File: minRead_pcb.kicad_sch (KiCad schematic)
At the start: 117 parts, among them J1 USB_C_Receptacle, J2 FH34SRJ-24S-0.5SH_50_, J3 FH34SRJ-6S-0.5SH_50_, J5 Conn_01x02, J7 Micro_SD_Card, Q10 BSS138, Q11 BSS138, Q16 MMBT3906, Q17 MMBT3904, Q18 AO3419, Q4 [BSS138] AO3400A, Q5 AO3419, Q6 AO3419, SW1 SW_Push, SW10 SW_Push, SW11 SW_Push, SW2 SW_Push, SW3 SW_Push, SW4 SW_Push, SW6 SW_Push, SW8 SW_Push, SW9 SW_Push, U1 TPD4E1U06DBVR, U11 AP3031KTR, U3 AP2112K-3.3, U4 ESP32-S3-WROOM-1, U6 TPD4E1U06DBVR, U7 MCP73832-2-OT

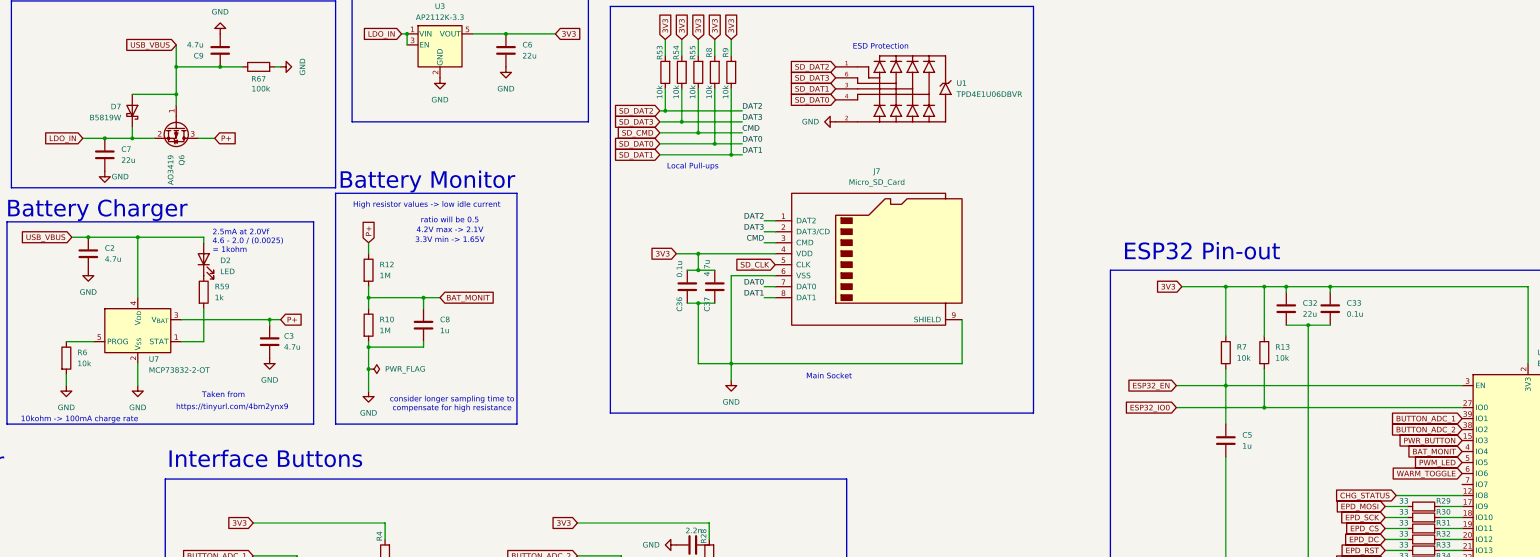
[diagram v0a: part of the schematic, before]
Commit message: implement charge pump
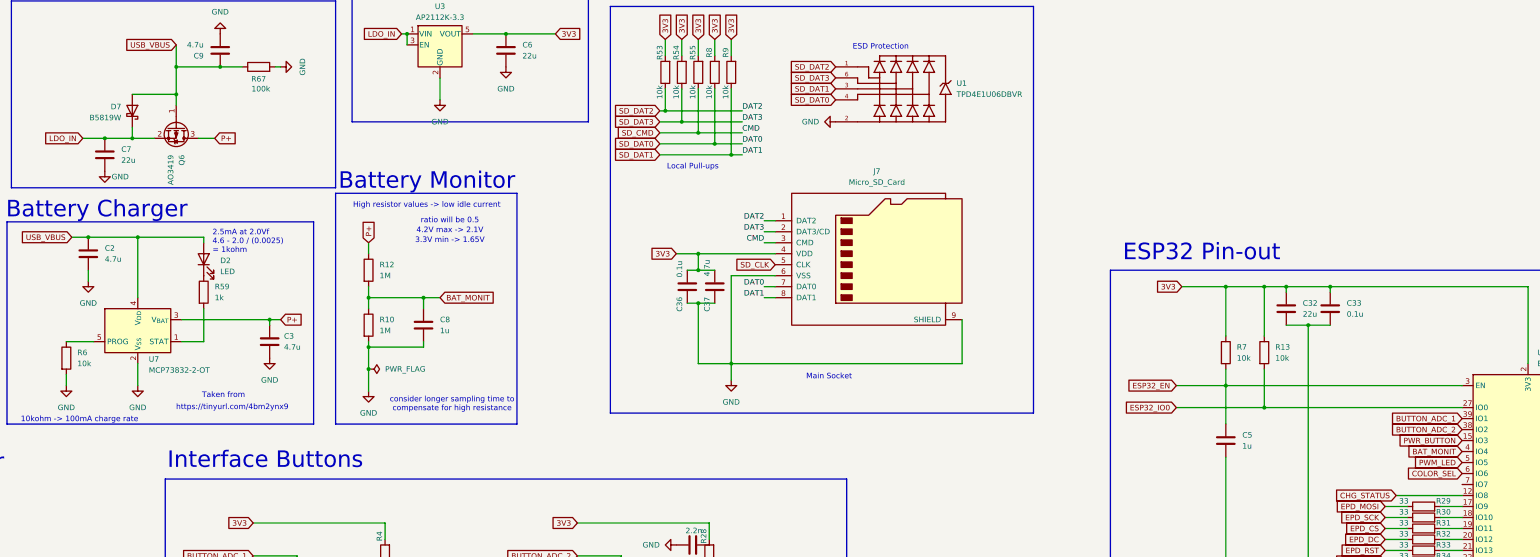
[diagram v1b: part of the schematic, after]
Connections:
- net WARM_TOGGLE is gone; now on net COLOR_SEL: U4.6 (IO6)
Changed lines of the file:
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@@
 	(wire
 		(pts
+			(xy 196.85 52.07) (xy 196.85 46.99)
+		)
+		(stroke
+			(width 0)
+			(type default)
+		)
+	)
+	(wire
+		(pts
 			(xy 261.62 266.7) (xy 264.16 266.7)
 		)
@@
 	(wire
 		(pts
+			(xy 115.57 93.98) (xy 115.57 91.44)
+		)
+		(stroke
+			(width 0)
+			(type default)
+		)
+	)
+	(wire
+		(pts
 			(xy 96.52 288.29) (xy 86.36 288.29)
 		)
@@
 		)
 	)
-	(global_label "PWR_BUTTON"
+	(global_label "COLOR_SEL"
 		(shape input)
-		(at 49.53 353.06 0)
+		(at 433.07 138.43 180)
 		(fields_autoplaced yes)
 		(effects
@@
 				(size 1.27 1.27)
 			)
-			(justify left)
+			(justify right)
 		)
 		(property "Intersheetrefs" "${INTERSHEET_REFS}"
-			(at 64.6709 353.06 0)
+			(at 419.5015 138.43 0)
 			(hide yes)
 			(show_name no)
@@
 					(size 1.27 1.27)
 				)
-				(justify left)
+				(justify right)
 			)
 		)
 	)
-	(global_label "ESP32_EN"
+	(global_label "PWR_BUTTON"
 		(shape input)
-		(at 367.03 118.11 180)
+		(at 49.53 353.06 0)
 		(fields_autoplaced yes)
 		(effects
@@
 				(size 1.27 1.27)
 			)
-			(justify right)
+			(justify left)
 		)
 		(property "Intersheetrefs" "${INTERSHEET_REFS}"
-			(at 359.5418 118.11 0)
+			(at 64.6709 353.06 0)
 			(hide yes)
 			(show_name no)
@@
 					(size 1.27 1.27)
 				)
-				(justify right)
+				(justify left)
 			)
 		)
 	)
-	(global_label "ESP32_IO0"
+	(global_label "ESP32_EN"
 		(shape input)
-		(at 367.03 123.19 180)
+		(at 367.03 118.11 180)
 		(fields_autoplaced yes)
 		(effects
@@
 		)
 		(property "Intersheetrefs" "${INTERSHEET_REFS}"
-			(at 353.8849 123.19 0)
+			(at 359.5418 118.11 0)
 			(hide yes)
 			(show_name no)
@@
 		)
 	)
-	(global_label "BUTTON_ADC_1"
+	(global_label "ESP32_IO0"
 		(shape input)
-		(at 433.07 125.73 180)
+		(at 367.03 123.19 180)
 		(fields_autoplaced yes)
 		(effects
@@
 		)
 		(property "Intersheetrefs" "${INTERSHEET_REFS}"
-			(at 416.1148 125.73 0)
+			(at 353.8849 123.19 0)
 			(hide yes)
 			(show_name no)
@@
 		)
 	)
-	(global_label "LED_SW"
+	(global_label "BUTTON_ADC_1"
 		(shape input)
-		(at 217.17 280.67 180)
+		(at 433.07 125.73 180)
 		(fields_autoplaced yes)
 		(effects
@@
 		)
 		(property "Intersheetrefs" "${INTERSHEET_REFS}"
-			(at 207.1092 280.67 0)
+			(at 416.1148 125.73 0)
 			(hide yes)
 			(show_name no)
@@
 		)
 	)
-	(global_label "WARM_TOGGLE"
+	(global_label "LED_SW"
 		(shape input)
-		(at 433.07 138.43 180)
+		(at 217.17 280.67 180)
 		(fields_autoplaced yes)
 		(effects
@@
 		)
 		(property "Intersheetrefs" "${INTERSHEET_REFS}"
-			(at 416.8406 138.43 0)
+			(at 207.1092 280.67 0)
 			(hide yes)
 			(show_name no)
@@
 		(length 2.54)
 		(shape round)
+		(at 196.85 50.8 270)
+		(fields_autoplaced yes)
+		(effects
+			(font
+				(size 1.27 1.27)
+			)
+			(justify right bottom)
+		)
+		(property "Netclass" "3V3"
+			(at 199.39 50.1015 90)
+			(show_name no)
+			(do_not_autoplace no)
+			(effects
+				(font
+					(size 1.27 1.27)
+				)
+				(justify left)
+			)
+		)
+		(property "Component Class" ""
+			(at -22.86 -199.39 0)
+			(show_name no)
+			(do_not_autoplace no)
+			(effects
+				(font
+					(size 1.27 1.27)
+					(italic yes)
+				)
+			)
+		)
+	)
+	(netclass_flag ""
+		(length 2.54)
+		(shape round)
 		(at 48.26 30.48 180)
 		(fields_autoplaced yes)
@@
 		(in_pos_files yes)
 		(dnp no)
-		(fields_autoplaced yes)
 		(property "Reference" "#PWR049"
 			(at 166.37 44.45 0)
@@
 	(symbol
 		(lib_id "power:GND")
-		(at 115.57 91.44 0)
+		(at 115.57 93.98 0)
 		(unit 1)
 		(body_style 1)
@@
 		(fields_autoplaced yes)
 		(property "Reference" "#PWR021"
-			(at 115.57 97.79 0)
+			(at 115.57 100.33 0)
 			(hide yes)
 			(show_name no)
@@
 		)
 		(property "Value" "GND"
-			(at 115.57 96.52 0)
+			(at 115.57 99.06 0)
 			(show_name no)
 			(do_not_autoplace no)
@@
 		)
 		(property "Footprint" ""
-			(at 115.57 91.44 0)
+			(at 115.57 93.98 0)
 			(hide yes)
 			(show_name no)
@@
 		)
 		(property "Datasheet" ""
-			(at 115.57 91.44 0)
+			(at 115.57 93.98 0)
 			(hide yes)
 			(show_name no)
@@
 		)
 		(property "Description" "Power symbol creates a global label with name \"GND\" , ground"
-			(at 115.57 91.44 0)
+			(at 115.57 93.98 0)
 			(hide yes)
 			(show_name no)
@@
 	(symbol
 		(lib_id "power:GND")
-		(at 196.85 46.99 0)
+		(at 196.85 52.07 0)
 		(unit 1)
 		(body_style 1)
@@
 		(fields_autoplaced yes)
 		(property "Reference" "#PWR027"
-			(at 196.85 53.34 0)
+			(at 196.85 58.42 0)
 			(hide yes)
 			(show_name no)
@@
 		)
 		(property "Value" "GND"
-			(at 196.85 52.07 0)
+			(at 196.85 57.15 0)
 			(show_name no)
 			(do_not_autoplace no)
@@
 		)
 		(property "Footprint" ""
-			(at 196.85 46.99 0)
+			(at 196.85 52.07 0)
 			(hide yes)
 			(show_name no)
@@
 		)
 		(property "Datasheet" ""
-			(at 196.85 46.99 0)
+			(at 196.85 52.07 0)
 			(hide yes)
 			(show_name no)
@@
 		)
 		(property "Description" "Power symbol creates a global label with name \"GND\" , ground"
-			(at 196.85 46.99 0)
+			(at 196.85 52.07 0)
 			(hide yes)
 			(show_name no)

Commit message: light bar circuit mostly routed
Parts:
- SW6: now fitted
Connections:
- net LED_PWR is gone; now on net LED_ACTIVATE: U4.10 (IO17)
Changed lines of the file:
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@@
 		)
 	)
-	(global_label "LED_PWR"
+	(global_label "LED_ACTIVATE"
 		(shape input)
 		(at 463.55 123.19 0)
@@
 		)
 		(property "Intersheetrefs" "${INTERSHEET_REFS}"
-			(at 474.9413 123.19 0)
+			(at 479.1747 123.19 0)
 			(hide yes)
 			(show_name no)
@@
 		(length 2.54)
 		(shape round)
-		(at 196.85 50.8 270)
-		(fields_autoplaced yes)
-		(effects
-			(font
-				(size 1.27 1.27)
-			)
-			(justify right bottom)
-		)
-		(property "Netclass" "3V3"
-			(at 199.39 50.1015 90)
-			(show_name no)
-			(do_not_autoplace no)
-			(effects
-				(font
-					(size 1.27 1.27)
-				)
-				(justify left)
-			)
-		)
-		(property "Component Class" ""
-			(at -22.86 -199.39 0)
-			(show_name no)
-			(do_not_autoplace no)
-			(effects
-				(font
-					(size 1.27 1.27)
-					(italic yes)
-				)
-			)
-		)
-	)
-	(netclass_flag ""
-		(length 2.54)
-		(shape round)
 		(at 48.26 30.48 180)
 		(fields_autoplaced yes)
@@
 		(length 2.54)
 		(shape round)
-		(at 293.37 299.72 180)
-		(fields_autoplaced yes)
-		(effects
-			(font
-				(size 1.27 1.27)
-			)
-			(justify right bottom)
-		)
-		(property "Netclass" "3V3"
-			(at 294.0685 302.26 0)
-			(show_name no)
-			(do_not_autoplace no)
-			(effects
-				(font
-					(size 1.27 1.27)
-				)
-				(justify left)
-			)
-		)
-		(property "Component Class" ""
-			(at 33.02 29.21 0)
-			(show_name no)
-			(do_not_autoplace no)
-			(effects
-				(font
-					(size 1.27 1.27)
-					(italic yes)
-				)
-			)
-		)
-	)
-	(netclass_flag ""
-		(length 2.54)
-		(shape round)
 		(at 66.04 288.29 90)
 		(fields_autoplaced yes)
@@
 		(length 2.54)
 		(shape round)
-		(at 66.04 270.51 90)
-		(fields_autoplaced yes)
-		(effects
-			(font
-				(size 1.27 1.27)
-			)
-			(justify left bottom)
-		)
-		(property "Netclass" "3V3"
-			(at 63.5 269.8115 90)
-			(show_name no)
-			(do_not_autoplace no)
-			(effects
-				(font
-					(size 1.27 1.27)
-				)
-				(justify left)
-			)
-		)
-		(property "Component Class" ""
-			(at -153.67 20.32 0)
-			(show_name no)
-			(do_not_autoplace no)
-			(effects
-				(font
-					(size 1.27 1.27)
-					(italic yes)
-				)
-			)
-		)
-	)
-	(netclass_flag ""
-		(length 2.54)
-		(shape round)
 		(at 58.42 30.48 180)
 		(fields_autoplaced yes)
@@
 		)
 	)
-	(netclass_flag ""
-		(length 2.54)
-		(shape round)
-		(at 346.71 299.72 0)
-		(fields_autoplaced yes)
-		(effects
-			(font
-				(size 1.27 1.27)
-			)
-			(justify left bottom)
-		)
-		(property "Netclass" "3V3"
-			(at 347.4085 297.18 0)
-			(show_name no)
-			(do_not_autoplace no)
-			(effects
-				(font
-					(size 1.27 1.27)
-				)
-				(justify left)
-			)
-		)
-		(property "Component Class" ""
-			(at 86.36 29.21 0)
-			(show_name no)
-			(do_not_autoplace no)
-			(effects
-				(font
-					(size 1.27 1.27)
-					(italic yes)
-				)
-			)
-		)
-	)
 	(symbol
 		(lib_id "Device:C")
@@
 		(on_board yes)
 		(in_pos_files yes)
-		(dnp yes)
+		(dnp no)
 		(fields_autoplaced yes)
 		(property "Reference" "SW6"

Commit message: reverse mount buttons
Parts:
- SW2, SW3, SW8, SW9: footprint mjtp1117:MJTP1117 -> DEAN:SKQGABE010_ALPS_Reverse
- SW6: footprint Button_Switch_THT:SW_PUSH_6mm -> Button_Switch_THT:SW_PUSH_1P1T_6x3.5mm_H4.3_APEM_MJTP1243; now not fitted
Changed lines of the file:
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@@
 	)
 	(symbol
+		(lib_name "SW_Push_1")
 		(lib_id "Switch:SW_Push")
 		(at 163.83 189.23 90)
@@
 			)
 		)
-		(property "Footprint" "mjtp1117:MJTP1117"
+		(property "Footprint" "DEAN:SKQGABE010_ALPS_Reverse"
 			(at 158.75 189.23 0)
 			(hide yes)
@@
 			)
 		)
-		(property "Footprint" "mjtp1117:MJTP1117"
+		(property "Footprint" "DEAN:SKQGABE010_ALPS_Reverse"
 			(at 172.72 189.23 0)
 			(hide yes)
@@
 			)
 		)
-		(property "Footprint" "mjtp1117:MJTP1117"
+		(property "Footprint" "DEAN:SKQGABE010_ALPS_Reverse"
 			(at 185.42 189.23 0)
 			(hide yes)
@@
 			)
 		)
-		(property "Footprint" "mjtp1117:MJTP1117"
+		(property "Footprint" "DEAN:SKQGABE010_ALPS_Reverse"
 			(at 196.85 189.23 0)
 			(hide yes)
@@
 		(on_board yes)
 		(in_pos_files yes)
-		(dnp no)
+		(dnp yes)
 		(fields_autoplaced yes)
 		(property "Reference" "SW6"
@@
 			)
 		)
-		(property "Footprint" "Button_Switch_THT:SW_PUSH_6mm"
+		(property "Footprint" "Button_Switch_THT:SW_PUSH_1P1T_6x3.5mm_H4.3_APEM_MJTP1243"
 			(at 107.95 347.98 0)
 			(hide yes)

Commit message: switch buttons to mid mount
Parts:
- added C12: 1u, Capacitor_SMD:C_0805_2012Metric_Pad1.18x1.45mm_HandSolder, symbol Device:C
- C6: value 22u -> 1u
- D2: footprint LED_THT:LED_D3.0mm -> LED_SMD:LED_0805_2012Metric_Pad1.15x1.40mm_HandSolder
- SW1, SW10, SW4: footprint mjtp1117:MJTP1117 -> DEAN:SKSNLAE010
- SW11: footprint mjtp1117:MJTP1117 -> TestPoint:TestPoint_Bridge_Pitch2.54mm_Drill1.0mm
- SW6: footprint Button_Switch_THT:SW_PUSH_1P1T_6x3.5mm_H4.3_APEM_MJTP1243 -> TestPoint:TestPoint_Bridge_Pitch2.54mm_Drill1.0mm
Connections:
- net GND: now also C12.2
- net LDO_IN: now also C12.1
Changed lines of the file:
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@@
 	)
 	(rectangle
-		(start 176.53 27.94)
+		(start 176.53 21.59)
 		(end 231.14 57.15)
 		(stroke
@@
 	(text "LDO 3.3V"
 		(exclude_from_sim no)
-		(at 177.292 25.654 0)
+		(at 177.038 16.002 0)
 		(effects
 			(font
@@
 	(wire
 		(pts
+			(xy 215.9 273.05) (xy 218.44 273.05)
+		)
+		(stroke
+			(width 0)
+			(type default)
+		)
+	)
+	(wire
+		(pts
 			(xy 142.24 100.33) (xy 142.24 107.95)
 		)
@@
 	(wire
 		(pts
-			(xy 217.17 283.21) (xy 218.44 283.21)
+			(xy 214.63 283.21) (xy 218.44 283.21)
 		)
 		(stroke
@@
 	(global_label "C-"
 		(shape input)
-		(at 218.44 273.05 180)
+		(at 215.9 273.05 180)
 		(fields_autoplaced yes)
 		(effects
@@
 		)
 		(property "Intersheetrefs" "${INTERSHEET_REFS}"
-			(at 212.6124 273.05 0)
+			(at 210.0724 273.05 0)
 			(hide yes)
 			(show_name no)
@@
 	(global_label "W-"
 		(shape input)
-		(at 217.17 283.21 180)
+		(at 214.63 283.21 180)
 		(fields_autoplaced yes)
 		(effects
@@
 		)
 		(property "Intersheetrefs" "${INTERSHEET_REFS}"
-			(at 211.161 283.21 0)
+			(at 208.621 283.21 0)
 			(hide yes)
 			(show_name no)
@@
 		(length 2.54)
 		(shape round)
-		(at 48.26 30.48 180)
-		(fields_autoplaced yes)
-		(effects
-			(font
-				(size 1.27 1.27)
-			)
-			(justify right bottom)
-		)
-		(property "Netclass" "3V3"
-			(at 48.9585 33.02 0)
-			(show_name no)
-			(do_not_autoplace no)
-			(effects
-				(font
-					(size 1.27 1.27)
-				)
-				(justify left)
-			)
-		)
-		(property "Component Class" ""
-			(at -171.45 -219.71 0)
-			(show_name no)
-			(do_not_autoplace no)
-			(effects
-				(font
-					(size 1.27 1.27)
-					(italic yes)
-				)
-			)
-		)
-	)
-	(netclass_flag ""
-		(length 2.54)
-		(shape round)
 		(at 284.48 266.7 180)
 		(fields_autoplaced yes)
@@
 		(length 2.54)
 		(shape round)
-		(at 304.8 289.56 0)
-		(fields_autoplaced yes)
-		(effects
-			(font
-				(size 1.27 1.27)
-			)
-			(justify left bottom)
-		)
-		(property "Netclass" "3V3"
-			(at 305.4985 287.02 0)
-			(show_name no)
-			(do_not_autoplace no)
-			(effects
-				(font
-					(size 1.27 1.27)
-				)
-				(justify left)
-			)
-		)
-		(property "Component Class" ""
-			(at 44.45 19.05 0)
-			(show_name no)
-			(do_not_autoplace no)
-			(effects
-				(font
-					(size 1.27 1.27)
-					(italic yes)
-				)
-			)
-		)
-	)
-	(netclass_flag ""
-		(length 2.54)
-		(shape round)
 		(at 49.53 297.18 0)
 		(fields_autoplaced yes)
@@
 			)
 		)
-		(property "Footprint" "mjtp1117:MJTP1117"
+		(property "Footprint" "TestPoint:TestPoint_Bridge_Pitch2.54mm_Drill1.0mm"
 			(at 109.22 372.11 0)
 			(hide yes)
@@
 			)
 		)
-		(property "Footprint" "mjtp1117:MJTP1117"
+		(property "Footprint" "DEAN:SKSNLAE010"
 			(at 233.68 189.23 0)
 			(hide yes)
@@
 	(symbol
 		(lib_id "power:GND")
+		(at 189.23 29.21 180)
+		(unit 1)
+		(body_style 1)
+		(exclude_from_sim no)
+		(in_bom yes)
+		(on_board yes)
+		(in_pos_files yes)
+		(dnp no)
+		(fields_autoplaced yes)
+		(property "Reference" "#PWR028"
+			(at 189.23 22.86 0)
+			(hide yes)
+			(show_name no)
+			(do_not_autoplace no)
+			(effects
+				(font
+					(size 1.27 1.27)
+				)
+			)
+		)
+		(property "Value" "GND"
+			(at 189.23 24.13 0)
+			(show_name no)
+			(do_not_autoplace no)
+			(effects
+				(font
+					(size 1.27 1.27)
+				)
+			)
+		)
+		(property "Footprint" ""
+			(at 189.23 29.21 0)
+			(hide yes)
+			(show_name no)
+			(do_not_autoplace no)
+			(effects
+				(font
+					(size 1.27 1.27)
+				)
+			)
+		)
+		(property "Datasheet" ""
+			(at 189.23 29.21 0)
+			(hide yes)
+			(show_name no)
+			(do_not_autoplace no)
+			(effects
+				(font
+					(size 1.27 1.27)
+				)
+			)
+		)
+		(property "Description" "Power symbol creates a global label with name \"GND\" , ground"
+			(at 189.23 29.21 0)
+			(hide yes)
+			(show_name no)
+			(do_not_autoplace no)
+			(effects
+				(font
+					(size 1.27 1.27)
+				)
+			)
+		)
+		(pin "1"
+		)
+		(instances
+			(project "minRead_pcb"
+				(path "/2fbd4c8f-b784-4d80-b374-4947df99a9bf"
+					(reference "#PWR028")
+					(unit 1)
+				)
+			)
+		)
+	)
+	(symbol
+		(lib_id "power:GND")
 		(at 156.21 163.83 270)
 		(unit 1)
@@
 			)
 		)
-		(property "Footprint" "LED_THT:LED_D3.0mm"
+		(property "Footprint" "LED_SMD:LED_0805_2012Metric_Pad1.15x1.40mm_HandSolder"
 			(at 142.24 88.9 0)
 			(hide yes)
@@
 			)
 		)
-		(property "Value" "22u"
+		(property "Value" "1u"
 			(at 215.9 41.9099 0)
 			(show_name no)
@@
 			)
 		)
-		(property "Footprint" "mjtp1117:MJTP1117"
+		(property "Footprint" "DEAN:SKSNLAE010"
 			(at 247.65 189.23 0)
 			(hide yes)
@@
 	(symbol
 		(lib_id "Device:C")
+		(at 189.23 33.02 180)
+		(unit 1)
+		(body_style 1)
+		(exclude_from_sim no)
+		(in_bom yes)
+		(on_board yes)
+		(in_pos_files yes)
+		(dnp no)
+		(property "Reference" "C12"
+			(at 183.134 30.48 0)
+			(show_name no)
+			(do_not_autoplace no)
+			(effects
+				(font
+					(size 1.27 1.27)
+				)
+				(justify right)
+			)
+		)
+		(property "Value" "1u"
+			(at 183.134 32.766 0)
+			(show_name no)
+			(do_not_autoplace no)
+			(effects
+				(font
+					(size 1.27 1.27)
+				)
+				(justify right)
+			)
+		)
+		(property "Footprint" "Capacitor_SMD:C_0805_2012Metric_Pad1.18x1.45mm_HandSolder"
+			(at 188.2648 29.21 0)
+			(hide yes)
+			(show_name no)
+			(do_not_autoplace no)
+			(effects
+				(font
+					(size 1.27 1.27)
+				)
+			)
+		)
+		(property "Datasheet" ""
+			(at 189.23 33.02 0)
+			(hide yes)
+			(show_name no)
+			(do_not_autoplace no)
+			(effects
+				(font
+					(size 1.27 1.27)
+				)
+			)
+		)
+		(property "Description" "Unpolarized capacitor"
+			(at 189.23 33.02 0)
+			(hide yes)
+			(show_name no)
+			(do_not_autoplace no)
+			(effects
+				(font
+					(size 1.27 1.27)
+				)
+			)
+		)
+		(pin "2"
+		)
+		(pin "1"
+		)
+		(instances
+			(project "minRead_pcb"
+				(path "/2fbd4c8f-b784-4d80-b374-4947df99a9bf"
+					(reference "C12")
+					(unit 1)
+				)
+			)
+		)
+	)
+	(symbol
+		(lib_id "Device:C")
 		(at 119.38 294.64 90)
 		(unit 1)
@@
 			)
 		)
-		(property "Footprint" "mjtp1117:MJTP1117"
+		(property "Footprint" "DEAN:SKSNLAE010"
 			(at 40.64 358.14 0)
 			(hide yes)
@@
 			)
 		)
-		(property "Footprint" "Button_Switch_THT:SW_PUSH_1P1T_6x3.5mm_H4.3_APEM_MJTP1243"
+		(property "Footprint" "TestPoint:TestPoint_Bridge_Pitch2.54mm_Drill1.0mm"
 			(at 107.95 347.98 0)
 			(hide yes)

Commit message: pre drs
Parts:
- removed C1: 1n, Capacitor_SMD:C_0805_2012Metric_Pad1.18x1.45mm_HandSolder, symbol Device:C
- removed C29: 2.2n, Capacitor_SMD:C_0805_2012Metric_Pad1.18x1.45mm_HandSolder, symbol Device:C
- removed H1, H2, H3, H4: MountingHole_Pad, MountingHole:MountingHole_2.2mm_M2_DIN965_Pad_TopBottom, symbol Mechanical:MountingHole_Pad
- removed R1: 1M, Resistor_SMD:R_0805_2012Metric_Pad1.20x1.40mm_HandSolder, symbol Device:R
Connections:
- net GND: now also J1.S1 (SHIELD)
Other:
- note removed: "Mounting"

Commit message: fin
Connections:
- net GND: now also J1.SH (SHIELD), J7.SH (SHIELD); no longer J1.S1 (SHIELD)
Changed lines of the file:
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@@
 	)
 	(junction
+		(at 317.5 106.68)
+		(diameter 0)
+		(color 0 0 0 0)
+	)
+	(junction
 		(at 378.46 118.11)
 		(diameter 0)
@@
 	(wire
 		(pts
+			(xy 321.31 97.79) (xy 321.31 106.68)
+		)
+		(stroke
+			(width 0)
+			(type default)
+		)
+	)
+	(wire
+		(pts
 			(xy 52.07 275.59) (xy 52.07 279.4)
 		)
@@
 	(wire
 		(pts
-			(xy 317.5 102.87) (xy 317.5 113.03)
+			(xy 317.5 102.87) (xy 317.5 106.68)
 		)
 		(stroke
@@
 	(wire
 		(pts
+			(xy 317.5 106.68) (xy 321.31 106.68)
+		)
+		(stroke
+			(width 0)
+			(type default)
+		)
+	)
+	(wire
+		(pts
 			(xy 256.54 113.03) (xy 264.16 113.03)
 		)
@@
 	(wire
 		(pts
+			(xy 317.5 97.79) (xy 321.31 97.79)
+		)
+		(stroke
+			(width 0)
+			(type default)
+		)
+	)
+	(wire
+		(pts
 			(xy 52.07 279.4) (xy 58.42 279.4)
 		)
@@
 	(wire
 		(pts
+			(xy 317.5 106.68) (xy 317.5 113.03)
+		)
+		(stroke
+			(width 0)
+			(type default)
+		)
+	)
+	(wire
+		(pts
 			(xy 224.79 334.01) (xy 227.33 334.01)
 		)
@@
 		(pin "B12"
 		)
-		(pin "S1"
+		(pin "SH"
 		)
 		(instances
@@
 		(pin "9"
 		)
+		(pin "SH"
+		)
 		(instances

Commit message: switch to 5k1 prog
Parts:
- R6: value 10k -> 5k1
- U7: value MCP73832-2-OT -> TP4054
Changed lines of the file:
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@@
 	)
 	(junction
-		(at 52.07 279.4)
-		(diameter 0)
-		(color 0 0 0 0)
-	)
-	(junction
 		(at 29.21 68.58)
 		(diameter 0)
@@
 	)
 	(junction
+		(at 66.04 270.51)
+		(diameter 0)
+		(color 0 0 0 0)
+	)
+	(junction
 		(at 163.83 170.18)
 		(diameter 0)
@@
 	)
 	(junction
+		(at 52.07 279.4)
+		(diameter 0)
+		(color 0 0 0 0)
+	)
+	(junction
 		(at 256.54 59.69)
 		(diameter 0)
@@
 	)
 	(junction
-		(at 66.04 288.29)
+		(at 248.92 54.61)
 		(diameter 0)
 		(color 0 0 0 0)
 	)
 	(junction
-		(at 248.92 54.61)
+		(at 279.4 266.7)
 		(diameter 0)
 		(color 0 0 0 0)
 	)
 	(junction
-		(at 279.4 266.7)
+		(at 184.15 170.18)
 		(diameter 0)
 		(color 0 0 0 0)
 	)
 	(junction
-		(at 184.15 170.18)
+		(at 66.04 288.29)
 		(diameter 0)
 		(color 0 0 0 0)
@@
 	)
 	(junction
-		(at 66.04 270.51)
-		(diameter 0)
-		(color 0 0 0 0)
-	)
-	(junction
 		(at 426.72 187.96)
 		(diameter 0)
@@
 			)
 		)
-		(property "Value" "MCP73832-2-OT"
+		(property "Value" "TP4054"
 			(at 129.54 114.554 0)
 			(show_name no)
@@
 			)
 		)
-		(property "Value" "10k"
+		(property "Value" "5k1"
 			(at 113.03 113.0299 0)
 			(show_name no)
